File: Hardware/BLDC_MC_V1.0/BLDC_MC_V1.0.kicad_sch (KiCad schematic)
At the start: 0 parts

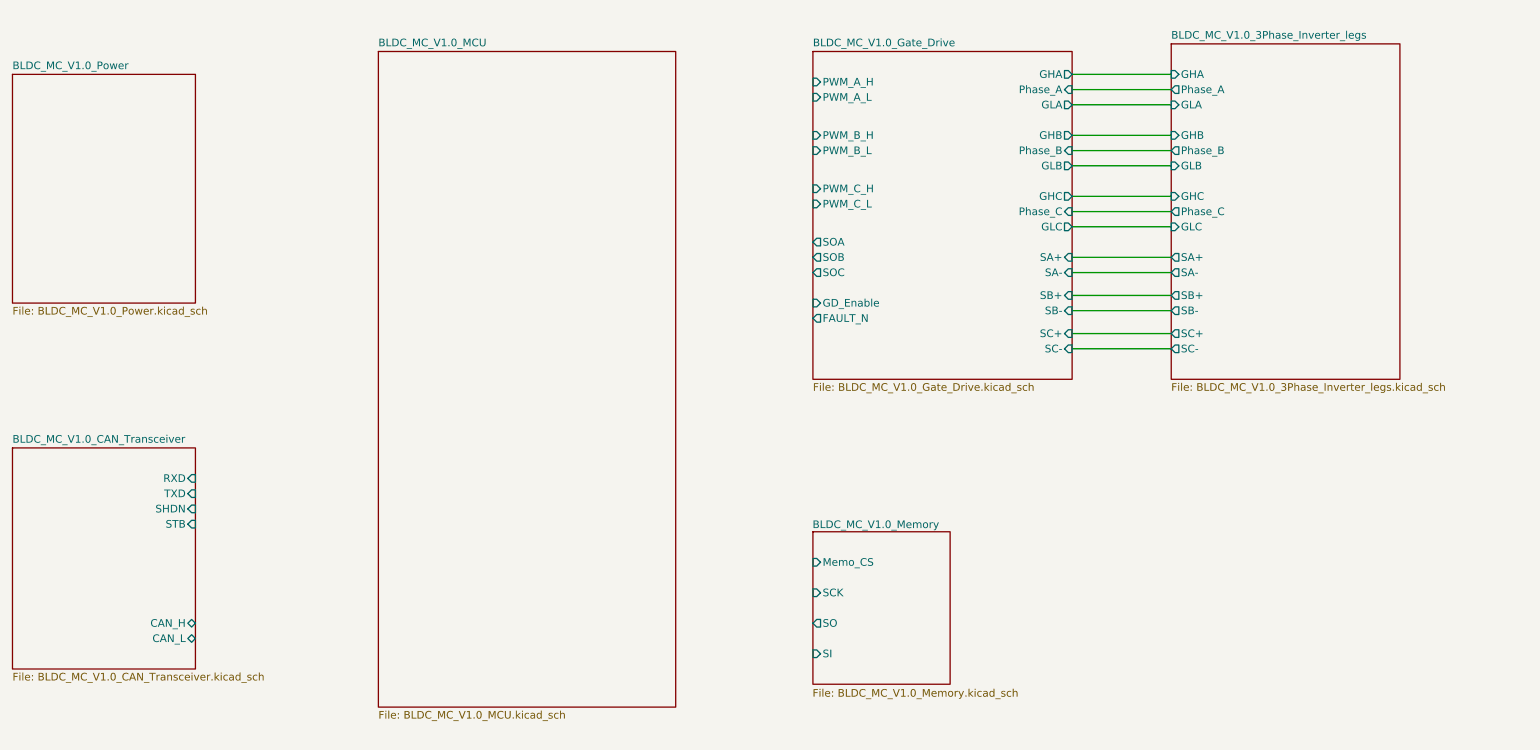
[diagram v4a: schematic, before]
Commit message: Edit Controller sheet and add oscillators for the controller
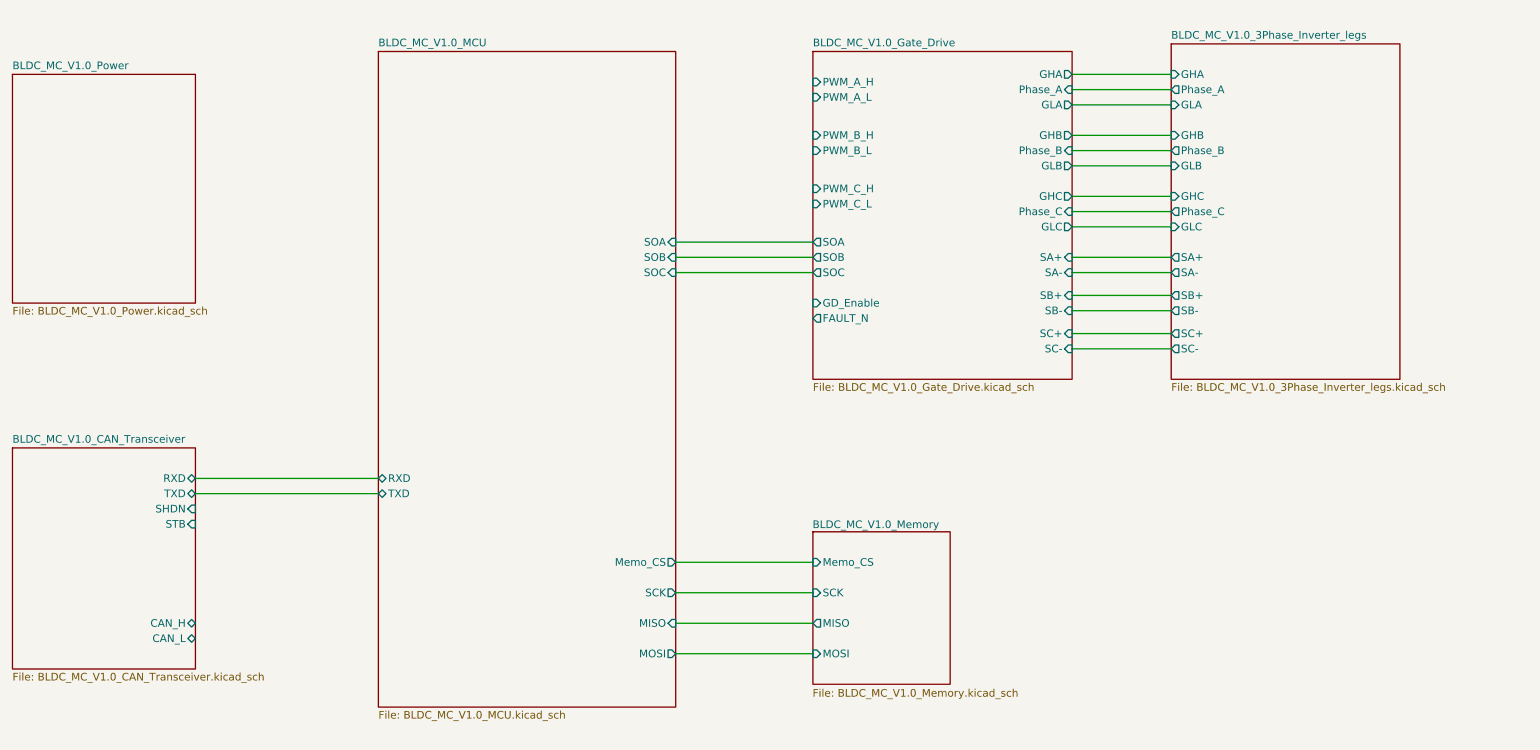
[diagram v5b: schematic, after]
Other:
- sheet BLDC_MC_V1.0_MCU ports: added MISO, MOSI, Memo_CS, RXD, SCK, SOA, SOB, SOC, TXD; removed none
- sheet BLDC_MC_V1.0_Memory ports: added MISO, MOSI; removed SI, SO
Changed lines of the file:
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@@
+	(wire
+		(pts
+			(xy 57.15 115.57) (xy 87.63 115.57)
+		)
+		(stroke
+			(width 0)
+			(type default)
+		)
+	)
 	(wire
 		(pts
@@
 	(wire
 		(pts
+			(xy 57.15 118.11) (xy 87.63 118.11)
+		)
+		(stroke
+			(width 0)
+			(type default)
+		)
+	)
+	(wire
+		(pts
 			(xy 203.2 85.09) (xy 219.71 85.09)
 		)
@@
 	(wire
 		(pts
+			(xy 137.16 134.62) (xy 160.02 134.62)
+		)
+		(stroke
+			(width 0)
+			(type default)
+		)
+	)
+	(wire
+		(pts
 			(xy 203.2 68.58) (xy 219.71 68.58)
 		)
@@
 	(wire
 		(pts
+			(xy 137.16 76.2) (xy 160.02 76.2)
+		)
+		(stroke
+			(width 0)
+			(type default)
+		)
+	)
+	(wire
+		(pts
 			(xy 203.2 78.74) (xy 219.71 78.74)
 		)
@@
 	(wire
 		(pts
+			(xy 137.16 144.78) (xy 160.02 144.78)
+		)
+		(stroke
+			(width 0)
+			(type default)
+		)
+	)
+	(wire
+		(pts
+			(xy 137.16 139.7) (xy 160.02 139.7)
+		)
+		(stroke
+			(width 0)
+			(type default)
+		)
+	)
+	(wire
+		(pts
+			(xy 137.16 81.28) (xy 160.02 81.28)
+		)
+		(stroke
+			(width 0)
+			(type default)
+		)
+	)
+	(wire
+		(pts
 			(xy 203.2 48.26) (xy 219.71 48.26)
+		)
+		(stroke
+			(width 0)
+			(type default)
+		)
+	)
+	(wire
+		(pts
+			(xy 137.16 78.74) (xy 160.02 78.74)
+		)
+		(stroke
+			(width 0)
+			(type default)
+		)
+	)
+	(wire
+		(pts
+			(xy 137.16 129.54) (xy 160.02 129.54)
 		)
 		(stroke
@@
 			)
 		)
-		(pin "RXD" input
+		(pin "RXD" bidirectional
 			(at 57.15 115.57 0)
 			(effects
@@
 			)
 		)
-		(pin "TXD" input
+		(pin "TXD" bidirectional
 			(at 57.15 118.11 0)
 			(effects
@@
 			)
 		)
+		(pin "TXD" bidirectional
+			(at 87.63 118.11 180)
+			(effects
+				(font
+					(size 1.27 1.27)
+				)
+				(justify left)
+			)
+		)
+		(pin "RXD" bidirectional
+			(at 87.63 115.57 180)
+			(effects
+				(font
+					(size 1.27 1.27)
+				)
+				(justify left)
+			)
+		)
+		(pin "SOA" input
+			(at 137.16 76.2 0)
+			(effects
+				(font
+					(size 1.27 1.27)
+				)
+				(justify right)
+			)
+		)
+		(pin "SOB" input
+			(at 137.16 78.74 0)
+			(effects
+				(font
+					(size 1.27 1.27)
+				)
+				(justify right)
+			)
+		)
+		(pin "SOC" input
+			(at 137.16 81.28 0)
+			(effects
+				(font
+					(size 1.27 1.27)
+				)
+				(justify right)
+			)
+		)
+		(pin "SCK" output
+			(at 137.16 134.62 0)
+			(effects
+				(font
+					(size 1.27 1.27)
+				)
+				(justify right)
+			)
+		)
+		(pin "MISO" input
+			(at 137.16 139.7 0)
+			(effects
+				(font
+					(size 1.27 1.27)
+				)
+				(justify right)
+			)
+		)
+		(pin "MOSI" output
+			(at 137.16 144.78 0)
+			(effects
+				(font
+					(size 1.27 1.27)
+				)
+				(justify right)
+			)
+		)
+		(pin "Memo_CS" output
+			(at 137.16 129.54 0)
+			(effects
+				(font
+					(size 1.27 1.27)
+				)
+				(justify right)
+			)
+		)
 		(instances
 			(project "BLDC_MC_V1.0"
@@
 			)
 		)
-		(pin "SI" input
+		(pin "MOSI" input
 			(at 160.02 144.78 180)
 			(effects
@@
 			)
 		)
-		(pin "SO" output
+		(pin "MISO" output
 			(at 160.02 139.7 180)
 			(effects

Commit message: Edit main sheet (root)
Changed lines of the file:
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@@
 	(wire
 		(pts
-			(xy 57.15 115.57) (xy 87.63 115.57)
+			(xy 77.47 115.57) (xy 87.63 115.57)
 		)
 		(stroke
@@
 	(wire
 		(pts
-			(xy 57.15 118.11) (xy 87.63 118.11)
+			(xy 77.47 118.11) (xy 87.63 118.11)
 		)
 		(stroke
@@
 	)
 	(sheet
-		(at 26.67 110.49)
+		(at 46.99 110.49)
 		(size 30.48 36.83)
 		(exclude_from_sim no)
@@
 		)
 		(fill
-			(color 0 0 0 0.0000)
+			(color 255 255 194 1.0000)
 		)
 		(property "Sheetname" "BLDC_MC_V1.0_CAN_Transceiver"
-			(at 26.67 109.7784 0)
+			(at 46.99 109.7784 0)
 			(effects
 				(font
@@
 		)
 		(property "Sheetfile" "BLDC_MC_V1.0_CAN_Transceiver.kicad_sch"
-			(at 26.67 147.9046 0)
+			(at 46.99 147.9046 0)
 			(effects
 				(font
@@
 		)
 		(pin "CAN_L" bidirectional
-			(at 57.15 142.24 0)
+			(at 77.47 142.24 0)
 			(effects
 				(font
@@
 		)
 		(pin "CAN_H" bidirectional
-			(at 57.15 139.7 0)
+			(at 77.47 139.7 0)
 			(effects
 				(font
@@
 		)
 		(pin "RXD" bidirectional
-			(at 57.15 115.57 0)
+			(at 77.47 115.57 0)
 			(effects
 				(font
@@
 		)
 		(pin "TXD" bidirectional
-			(at 57.15 118.11 0)
+			(at 77.47 118.11 0)
 			(effects
 				(font
@@
 		)
 		(pin "SHDN" input
-			(at 57.15 120.65 0)
+			(at 77.47 120.65 0)
 			(effects
 				(font
@@
 		)
 		(pin "STB" input
-			(at 57.15 123.19 0)
+			(at 77.47 123.19 0)
 			(effects
 				(font
@@
 		)
 		(fill
-			(color 0 0 0 0.0000)
+			(color 255 255 194 1.0000)
 		)
 		(property "Sheetname" "BLDC_MC_V1.0_Gate_Drive"
@@
 	)
 	(sheet
-		(at 219.71 43.18)
-		(size 38.1 55.88)
+		(at 219.71 44.45)
+		(size 38.1 54.61)
 		(exclude_from_sim no)
 		(in_bom yes)
@@
 		)
 		(fill
-			(color 0 0 0 0.0000)
+			(color 255 255 194 1.0000)
 		)
 		(property "Sheetname" "BLDC_MC_V1.0_3Phase_Inverter_legs"
-			(at 219.71 42.4684 0)
+			(at 219.71 43.7384 0)
 			(effects
 				(font
@@
 		)
 		(fill
-			(color 0 0 0 0.0000)
+			(color 255 255 194 1.0000)
 		)
 		(property "Sheetname" "BLDC_MC_V1.0_MCU"
@@
 		)
 		(fill
-			(color 0 0 0 0.0000)
+			(color 255 255 194 1.0000)
 		)
 		(property "Sheetname" "BLDC_MC_V1.0_Memory"
@@
 	)
 	(sheet
-		(at 26.67 48.26)
+		(at 46.99 53.34)
 		(size 30.48 38.1)
 		(exclude_from_sim no)
@@
 		)
 		(fill
-			(color 0 0 0 0.0000)
+			(color 255 255 194 1.0000)
 		)
 		(property "Sheetname" "BLDC_MC_V1.0_Power"
-			(at 26.67 47.5484 0)
+			(at 46.99 52.6284 0)
 			(effects
 				(font
@@
 		)
 		(property "Sheetfile" "BLDC_MC_V1.0_Power.kicad_sch"
-			(at 26.67 86.9446 0)
-			(effects
-				(font
+			(at 46.99 92.0246 0)
+			(effects
+				(font

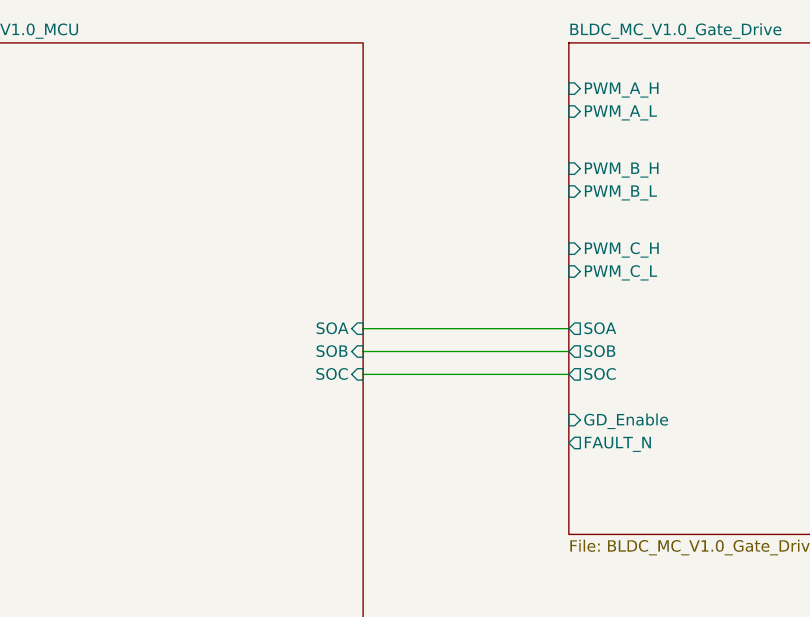
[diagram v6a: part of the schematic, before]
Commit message: Add the USB-C connector - define the PWM pins and other enable and fault pins for gate driver
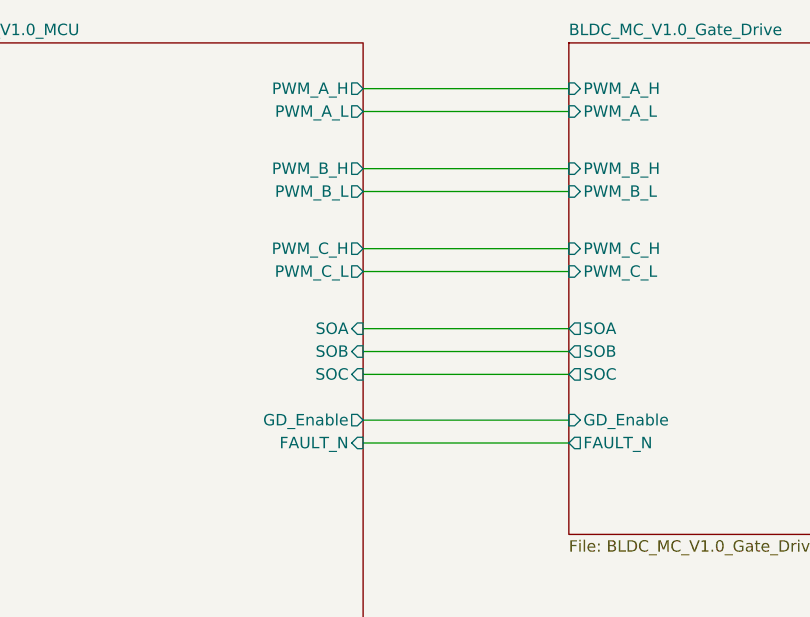
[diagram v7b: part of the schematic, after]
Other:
- sheet BLDC_MC_V1.0_MCU ports: added FAULT_N, GD_Enable, PWM_A_H, PWM_A_L, PWM_B_H, PWM_B_L, PWM_C_H, PWM_C_L; removed none
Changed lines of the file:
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@@
+	(wire
+		(pts
+			(xy 137.16 58.42) (xy 160.02 58.42)
+		)
+		(stroke
+			(width 0)
+			(type default)
+		)
+	)
 	(wire
 		(pts
@@
 	(wire
 		(pts
+			(xy 137.16 60.96) (xy 160.02 60.96)
+		)
+		(stroke
+			(width 0)
+			(type default)
+		)
+	)
+	(wire
+		(pts
+			(xy 137.16 86.36) (xy 160.02 86.36)
+		)
+		(stroke
+			(width 0)
+			(type default)
+		)
+	)
+	(wire
+		(pts
 			(xy 203.2 60.96) (xy 219.71 60.96)
 		)
@@
 	(wire
 		(pts
+			(xy 137.16 69.85) (xy 160.02 69.85)
+		)
+		(stroke
+			(width 0)
+			(type default)
+		)
+	)
+	(wire
+		(pts
+			(xy 137.16 67.31) (xy 160.02 67.31)
+		)
+		(stroke
+			(width 0)
+			(type default)
+		)
+	)
+	(wire
+		(pts
+			(xy 137.16 88.9) (xy 160.02 88.9)
+		)
+		(stroke
+			(width 0)
+			(type default)
+		)
+	)
+	(wire
+		(pts
 			(xy 137.16 81.28) (xy 160.02 81.28)
 		)
@@
 	(wire
 		(pts
+			(xy 137.16 49.53) (xy 160.02 49.53)
+		)
+		(stroke
+			(width 0)
+			(type default)
+		)
+	)
+	(wire
+		(pts
 			(xy 203.2 48.26) (xy 219.71 48.26)
+		)
+		(stroke
+			(width 0)
+			(type default)
+		)
+	)
+	(wire
+		(pts
+			(xy 137.16 52.07) (xy 160.02 52.07)
 		)
 		(stroke
@@
 			(effects
 				(font
+					(size 1.27 1.27)
+				)
+				(justify right)
+			)
+		)
+		(pin "FAULT_N" input
+			(at 137.16 88.9 0)
+			(effects
+				(font
+					(size 1.27 1.27)
+				)
+				(justify right)
+			)
+		)
+		(pin "GD_Enable" output
+			(at 137.16 86.36 0)
+			(effects
+				(font
+					(size 1.27 1.27)
+				)
+				(justify right)
+			)
+		)
+		(pin "PWM_A_L" output
+			(at 137.16 52.07 0)
+			(effects
+				(font
+					(size 1.27 1.27)
+				)
+				(justify right)
+			)
+		)
+		(pin "PWM_C_L" output
+			(at 137.16 69.85 0)
+			(effects
+				(font
+					(size 1.27 1.27)
+				)
+				(justify right)
+			)
+		)
+		(pin "PWM_C_H" output
+			(at 137.16 67.31 0)
+			(effects
+				(font
+					(size 1.27 1.27)
+				)
+				(justify right)
+			)
+		)
+		(pin "PWM_A_H" output
+			(at 137.16 49.53 0)
+			(effects
+				(font
+					(size 1.27 1.27)
+				)
+				(justify right)
+			)
+		)
+		(pin "PWM_B_H" output
+			(at 137.16 58.42 0)
+			(effects
+				(font
+					(size 1.27 1.27)
+				)
+				(justify right)
+			)
+		)
+		(pin "PWM_B_L" output
+			(at 137.16 60.96 0)
+			(effects
+				(font

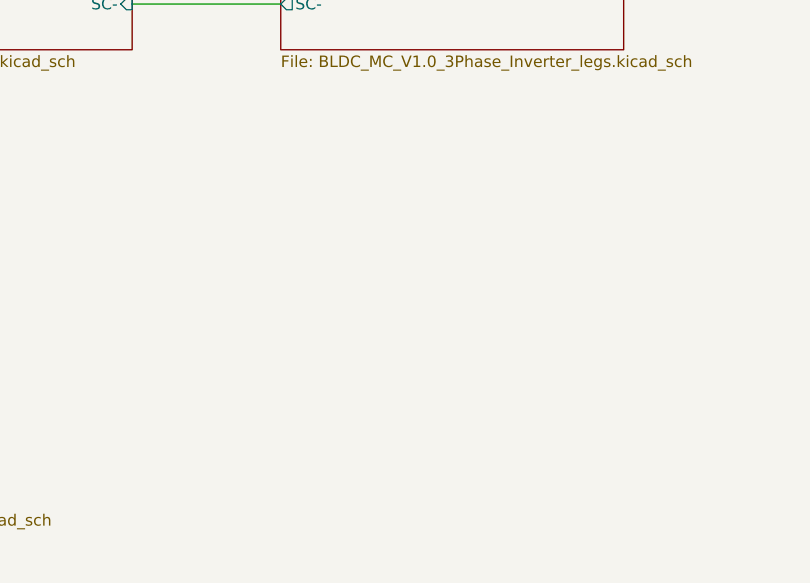
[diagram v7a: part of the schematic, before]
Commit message: Add hall sensor sheet and its simulation file
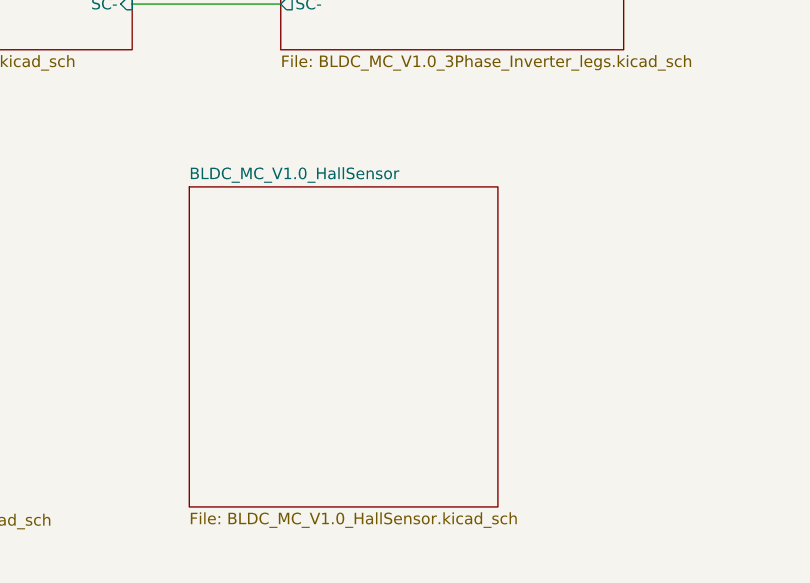
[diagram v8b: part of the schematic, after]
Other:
- added sheet BLDC_MC_V1.0_HallSensor (BLDC_MC_V1.0_HallSensor.kicad_sch)
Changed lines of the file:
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@@
+	)
+	(sheet
+		(at 209.55 114.3)
+		(size 34.29 35.56)
+		(exclude_from_sim no)
+		(in_bom yes)
+		(on_board yes)
+		(dnp no)
+		(fields_autoplaced yes)
+		(stroke
+			(width 0.1524)
+			(type solid)
+		)
+		(fill
+			(color 255 255 194 1.0000)
+		)
+		(property "Sheetname" "BLDC_MC_V1.0_HallSensor"
+			(at 209.55 113.5884 0)
+			(effects
+				(font
+					(size 1.27 1.27)
+				)
+				(justify left bottom)
+			)
+		)
+		(property "Sheetfile" "BLDC_MC_V1.0_HallSensor.kicad_sch"
+			(at 209.55 150.4446 0)
+			(effects
+				(font
+					(size 1.27 1.27)
+				)
+				(justify left top)
+			)
+		)
+		(instances
+			(project "BLDC_MC_V1.0"
+				(path "/e34fda66-7244-4ac9-bbf7-3725f03e688f"
+					(page "8")
+				)
+			)
+		)
 	)
 	(sheet
